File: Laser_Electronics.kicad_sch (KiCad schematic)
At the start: 36 parts, among them J1 MOT_X, J2 UART, J3 LIM_X, J4 LASER, J5 POWER, J6 GPIO, J7 MOT_Y, J8 LIM_Y, J9 Micro_SD_Card, Q1 BC848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

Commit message: ver 1 layout
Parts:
- added C13: 100n, Capacitor_SMD:C_0603_1608Metric, symbol Device:C
- added D2: LED-WS2812B, LED_SMD:LED_Cree-PLCC4_2x2mm_CW, symbol !moje:LED-WS2812B
- added H1: MountingHole_Pad, MountingHole:MountingHole_3.2mm_M3_DIN965_Pad, symbol Mechanical:MountingHole_Pad
- added J11: LED2, Connector_PinHeader_2.54mm:PinHeader_1x03_P2.54mm_Vertical, symbol Connector:Conn_01x03_Pin
- added J9: UDPI, Connector_PinHeader_2.54mm:PinHeader_1x04_P2.54mm_Vertical, symbol Connector:Conn_01x04_Pin
- added R7: 3k9, Resistor_SMD:R_0603_1608Metric, symbol Device:R
- added U3: ATtiny412-SS, Package_SO:SOIC-8_3.9x4.9mm_P1.27mm, symbol MCU_Microchip_ATtiny:ATtiny412-SS
- C11, C4, C6, C8: footprint Capacitor_SMD:C_0805_2012Metric -> Capacitor_SMD:CP_Elec_6.3x7.7
- J10: renamed from J8; footprint Connector_JST:JST_EH_B2B-EH-A_1x02_P2.50mm_Vertical -> Connector_JST:JST_PH_B2B-PH-K_1x02_P2.00mm_Vertical
- J4: renamed from J3; footprint Connector_JST:JST_EH_B2B-EH-A_1x02_P2.50mm_Vertical -> Connector_JST:JST_PH_B2B-PH-K_1x02_P2.00mm_Vertical
- J7: renamed from J9; value Micro_SD_Card -> Micro_SD; footprint Connector_Card:microSD_HC_Hirose_DM3BT-DSF-PEJS -> !moje:J_SD_Card-micro_socket_A
- U1: value ESP32-WROOM-32 -> ESP32-WROOM
- renumbered J6 to J2, J2 to J3, J4 to J5, J5 to J6, J7 to J8
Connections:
- net +3.3V: now also J3.3 (Pin_3), C13.2, D2.4 (Vdd), J11.3 (Pin_3), J9.4 (Pin_4), U3.1 (VCC)
- net GND: now also C13.1, D2.2 (Vss), H1.1, J11.1 (Pin_1), J9.1 (Pin_1), U3.8 (GND)
- net io02: now also U3.4 (PA1)
- net cts: now reaches J3.2 (Pin_2), Q1.2 (E), R5.1
- net rts: now reaches J3.6 (Pin_6), Q2.2 (E), R4.1
- net at A1.3 (A2): now also J1.1 (Pin_1); no longer J1.2 (Pin_2)
- net at A1.4 (A1): now also J1.2 (Pin_2); no longer J1.1 (Pin_1)
- net at A2.3 (A2): now also J8.1 (Pin_1); no longer J8.2 (Pin_2)
- net at A2.4 (A1): now also J8.2 (Pin_2); no longer J8.1 (Pin_1)
- net io0 renamed io00
- net io00: now also J9.2 (Pin_2), R7.2, U3.6 (~{RESET}/PA0)
- new net: D2.3 (Di), U3.7 (PA3)
- new net: D2.1 (Do), J11.2 (Pin_2)
- new net rx412: J9.3 (Pin_3), R7.1
- no-connect marks 13 -> 15
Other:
- moved on the sheet: C12, J2, J7

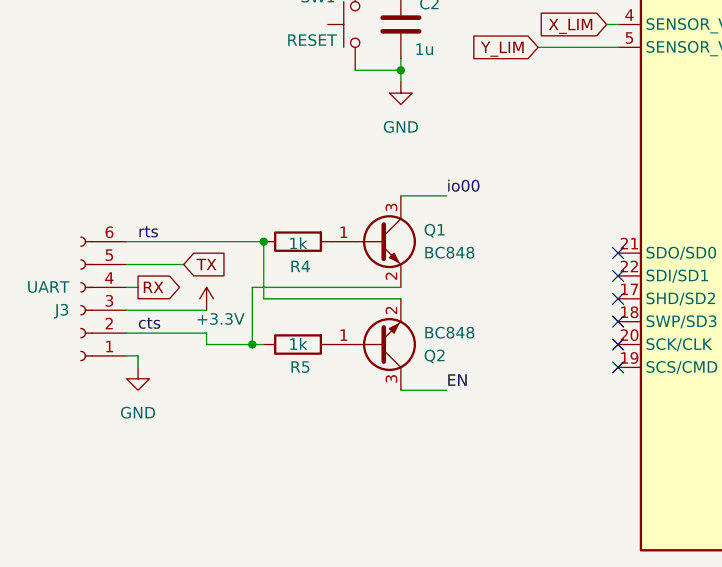
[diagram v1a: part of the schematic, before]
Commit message: UART reset circuit error repaired
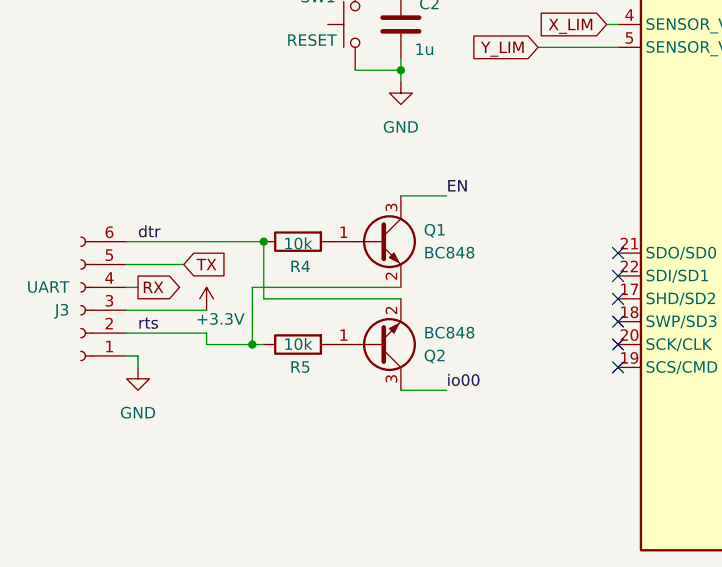
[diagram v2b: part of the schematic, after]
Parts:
- R4, R5: value 1k -> 10k
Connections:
- net cts is gone; now on net rts: J3.2 (Pin_2), Q1.2 (E), R5.1
- net EN: now also Q1.3 (C); no longer Q2.3 (C)
- net io00: now also Q2.3 (C); no longer Q1.3 (C)
- net rts: no longer J3.6 (Pin_6), Q2.2 (E), R4.1
- new net dtr: J3.6 (Pin_6), Q2.2 (E), R4.1
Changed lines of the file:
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@@
 	(title_block
 		(title "Laser Cutter Flow NC control board")
-		(date "2025-10-12")
-		(rev "v1")
+		(date "2025-10-27")
+		(rev "2")
 		(company "© JaSoSe 2025")
 	)
@@
 	(wire
 		(pts
-			(xy 58.42 77.47) (xy 63.5 77.47)
-		)
-		(stroke
-			(width 0)
-			(type default)
-		)
-	)
-	(wire
-		(pts
 			(xy 87.63 116.84) (xy 86.36 116.84)
 		)
@@
 	(wire
 		(pts
-			(xy 228.6 148.59) (xy 229.87 148.59)
+			(xy 58.42 77.47) (xy 63.5 77.47)
 		)
 		(stroke
@@
 	(wire
 		(pts
-			(xy 232.41 34.29) (xy 232.41 35.56)
+			(xy 228.6 148.59) (xy 229.87 148.59)
 		)
 		(stroke
@@
 	(wire
 		(pts
-			(xy 232.41 106.68) (xy 232.41 113.03)
+			(xy 232.41 34.29) (xy 232.41 35.56)
 		)
 		(stroke
@@
 	(wire
 		(pts
-			(xy 227.33 39.37) (xy 227.33 41.91)
+			(xy 232.41 106.68) (xy 232.41 113.03)
 		)
 		(stroke
@@
 	(wire
 		(pts
-			(xy 248.92 64.77) (xy 248.92 67.31)
+			(xy 227.33 39.37) (xy 227.33 41.91)
 		)
 		(stroke
@@
 	(wire
 		(pts
-			(xy 58.42 55.88) (xy 63.5 55.88)
+			(xy 248.92 64.77) (xy 248.92 67.31)
 		)
 		(stroke
@@
 	(wire
 		(pts
+			(xy 58.42 55.88) (xy 63.5 55.88)
+		)
+		(stroke
+			(width 0)
+			(type default)
+		)
+	)
+	(wire
+		(pts
 			(xy 53.34 31.75) (xy 58.42 31.75)
 		)
@@
 	)
 	(label "io00"
-		(at 63.5 55.88 0)
+		(at 63.5 77.47 0)
 		(effects
 			(font
@@
 		)
 	)
-	(label "cts"
+	(label "rts"
 		(at 29.21 71.12 0)
 		(effects
@@
 	)
 	(label "EN"
-		(at 63.5 77.47 0)
+		(at 63.5 55.88 0)
 		(effects
 			(font
@@
 		)
 	)
-	(label "rts"
+	(label "dtr"
 		(at 29.21 60.96 0)
 		(effects
@@
 			)
 		)
-		(property "Value" "1k"
+		(property "Value" "10k"
 			(at 46.99 61.214 90)
 			(effects
@@
 			)
 		)
-		(property "Value" "1k"
+		(property "Value" "10k"
 			(at 46.99 72.39 90)
 			(effects
